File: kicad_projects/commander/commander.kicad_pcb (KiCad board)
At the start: 2 copper layers, 50 x 70 mm, 17 parts, among them J1 left input IDC14, J2 right input IDC14, J4 TPS pinout, J5 DS1020-12-6VBT1A-R, J6 PSP 3000 connector SFV4R-4STB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, J7 PSP 2000 raw pins out, J8 debug out, SW1 RESET_SWITCH, U1 Pico, U2 AQY212S

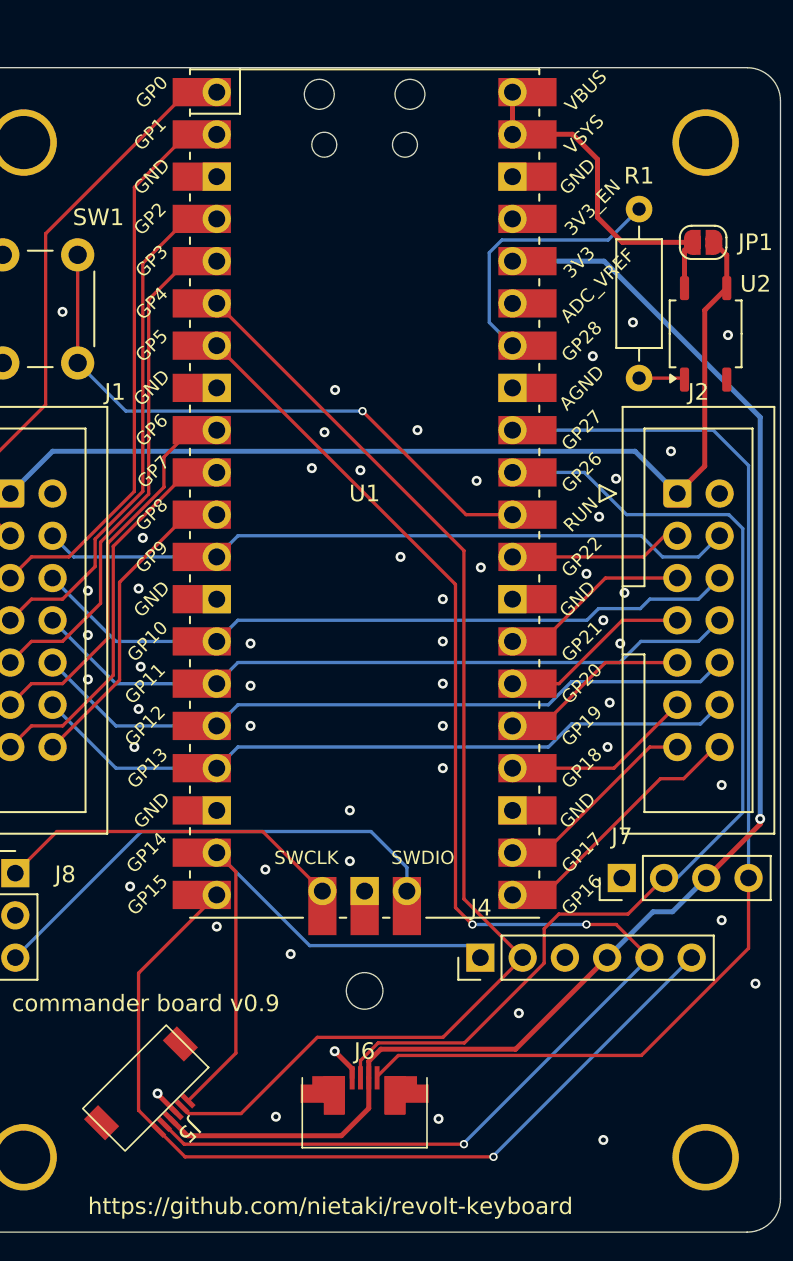
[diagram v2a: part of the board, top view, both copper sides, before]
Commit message: Clean up some vias, 0.25mm spacing of power nets for cleaner zone fills
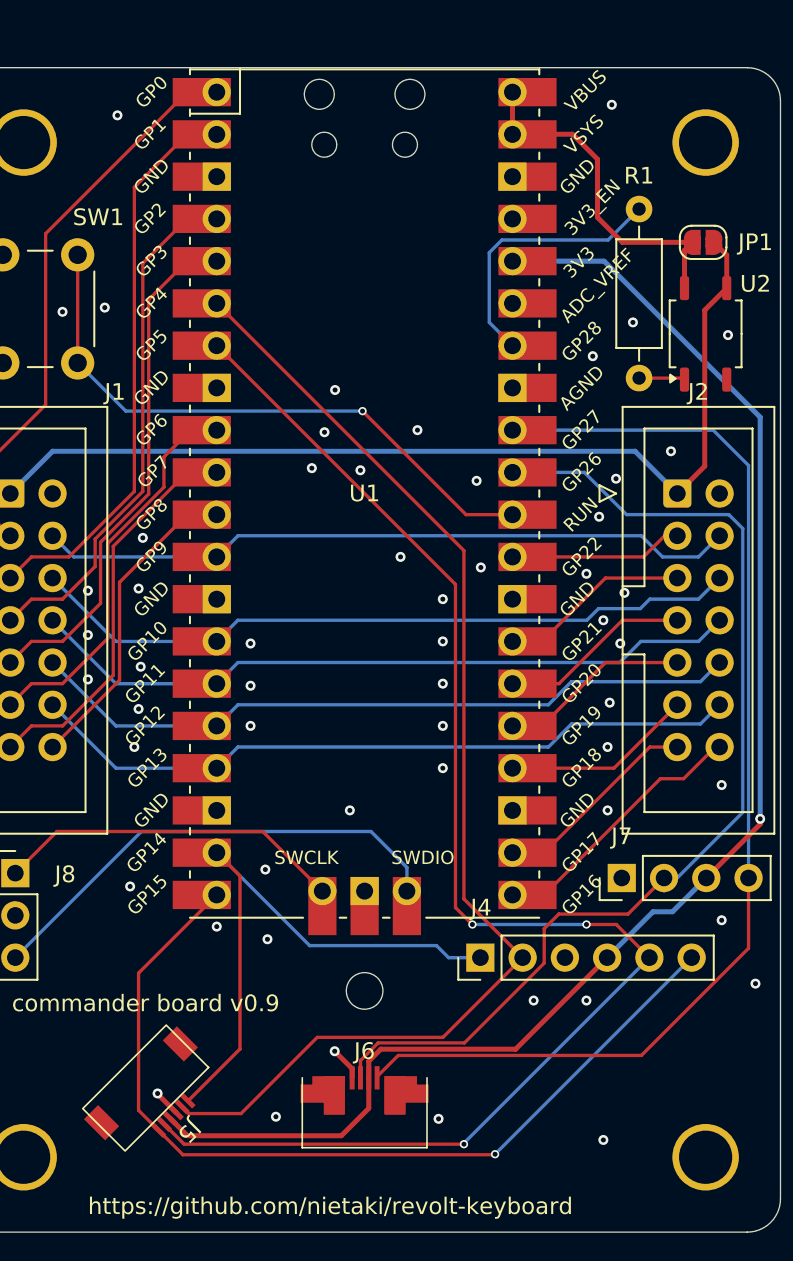
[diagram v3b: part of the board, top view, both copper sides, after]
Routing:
- net GND: vias 52 -> 56
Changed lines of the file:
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@@
   (segment (start 149 65.5) (end 149 69) (width 0.3) (layer "F.Cu") (net 26))
   (segment (start 154.23 70.97) (end 154.23 73.25) (width 0.3) (layer "F.Cu") (net 26))
-  (segment (start 127.26 108.34) (end 127.26 119.24) (width 0.2) (layer "F.Cu") (net 27))
-  (segment (start 127.26 119.24) (end 124.383883 122.116117) (width 0.2) (layer "F.Cu") (net 27))
-  (segment (start 126.11 107.19) (end 127.26 108.34) (width 0.2) (layer "F.Cu") (net 27))
+  (segment (start 127.508 108.588) (end 127.508 118.992) (width 0.2) (layer "F.Cu") (net 27))
+  (segment (start 126.11 107.19) (end 127.508 108.588) (width 0.2) (layer "F.Cu") (net 27))
+  (segment (start 127.508 118.992) (end 124.383883 122.116117) (width 0.2) (layer "F.Cu") (net 27))
   (segment (start 126.11 107.19) (end 131.696 112.776) (width 0.2) (layer "B.Cu") (net 27))
-  (segment (start 131.696 112.776) (end 141.236 112.776) (width 0.2) (layer "B.Cu") (net 27))
-  (segment (start 141.236 112.776) (end 141.96 113.5) (width 0.2) (layer "B.Cu") (net 27))
+  (segment (start 131.696 112.776) (end 139.319 112.776) (width 0.2) (layer "B.Cu") (net 27))
+  (segment (start 140.043 113.5) (end 141.96 113.5) (width 0.2) (layer "B.Cu") (net 27))
+  (segment (start 139.319 112.776) (end 140.043 113.5) (width 0.2) (layer "B.Cu") (net 27))
   (segment (start 127.568264 122.875736) (end 124.436396 122.875736) (width 0.2) (layer "F.Cu") (net 28))
   (segment (start 124.436396 122.875736) (end 124.03033 122.46967) (width 0.2) (layer "F.Cu") (net 28))
@@
   (via (at 116.84 74.676) (size 0.6) (drill 0.3) (layers "F.Cu" "B.Cu") (net 29))
   (via (at 156.464 103.124) (size 0.6) (drill 0.3) (layers "F.Cu" "B.Cu") (net 29))
-  (via (at 144.272 116.84) (size 0.6) (drill 0.3) (layers "F.Cu" "B.Cu") (net 29))
+  (via (at 149.606 104.648) (size 0.6) (drill 0.3) (layers "F.Cu" "B.Cu") (net 29))
   (via (at 122.555 121.666) (size 0.6) (drill 0.3) (layers "F.Cu" "B.Cu") (net 29))
   (via (at 139.7 99.568) (size 0.6) (drill 0.3) (layers "F.Cu" "B.Cu") (net 29))
+  (via (at 145.161 116.078) (size 0.6) (drill 0.3) (layers "F.Cu" "B.Cu") (net 29))
   (via (at 138.176 81.788) (size 0.6) (drill 0.3) (layers "F.Cu" "B.Cu") (net 29))
   (via (at 150.114 84.709) (size 0.6) (drill 0.3) (layers "F.Cu" "B.Cu") (net 29))
@@
   (via (at 139.7 97.028) (size 0.6) (drill 0.3) (layers "F.Cu" "B.Cu") (net 29))
   (via (at 126.111 111.633) (size 0.6) (drill 0.3) (layers "F.Cu" "B.Cu") (net 29))
-  (via (at 134.112 107.696) (size 0.6) (drill 0.3) (layers "F.Cu" "B.Cu") (net 29))
   (via (at 131.826 84.074) (size 0.6) (drill 0.3) (layers "F.Cu" "B.Cu") (net 29))
   (via (at 129.667 123.063) (size 0.6) (drill 0.3) (layers "F.Cu" "B.Cu") (net 29))
@@
   (via (at 148.717 77.343) (size 0.6) (drill 0.3) (layers "F.Cu" "B.Cu") (net 29))
   (via (at 121.539 96.012) (size 0.6) (drill 0.3) (layers "F.Cu" "B.Cu") (net 29))
-  (via (at 130.556 113.284) (size 0.6) (drill 0.3) (layers "F.Cu" "B.Cu") (net 29))
+  (via (at 129.159 112.395) (size 0.6) (drill 0.3) (layers "F.Cu" "B.Cu") (net 29))
   (via (at 149.098 86.995) (size 0.6) (drill 0.3) (layers "F.Cu" "B.Cu") (net 29))
   (via (at 128.143 94.615) (size 0.6) (drill 0.3) (layers "F.Cu" "B.Cu") (net 29))
@@
   (via (at 149.733 98.171) (size 0.6) (drill 0.3) (layers "F.Cu" "B.Cu") (net 29))
   (via (at 139.446 123.19) (size 0.6) (drill 0.3) (layers "F.Cu" "B.Cu") (net 29))
+  (via (at 148.336 116.078) (size 0.6) (drill 0.3) (layers "F.Cu" "B.Cu") (net 29))
   (via (at 129.032 108.204) (size 0.6) (drill 0.3) (layers "F.Cu" "B.Cu") (net 29))
   (via (at 118.364 91.44) (size 0.6) (drill 0.3) (layers "F.Cu" "B.Cu") (net 29))
@@
   (via (at 132.588 81.915) (size 0.6) (drill 0.3) (layers "F.Cu" "B.Cu") (net 29))
   (via (at 151.13 75.311) (size 0.6) (drill 0.3) (layers "F.Cu" "B.Cu") (net 29))
+  (via (at 119.38 74.422) (size 0.6) (drill 0.3) (layers "F.Cu" "B.Cu") (net 29))
   (via (at 128.143 99.568) (size 0.6) (drill 0.3) (layers "F.Cu" "B.Cu") (net 29))
+  (via (at 149.86 62.23) (size 0.6) (drill 0.3) (layers "F.Cu" "B.Cu") (net 29))
   (via (at 121.666 88.265) (size 0.6) (drill 0.3) (layers "F.Cu" "B.Cu") (net 29))
   (via (at 149.352 93.218) (size 0.6) (drill 0.3) (layers "F.Cu" "B.Cu") (net 29))
   (via (at 133.201 119.126) (size 0.6) (drill 0.3) (layers "F.Cu" "B.Cu") (net 29))
   (via (at 121.158 100.838) (size 0.6) (drill 0.3) (layers "F.Cu" "B.Cu") (net 29))
+  (via (at 120.142 62.865) (size 0.6) (drill 0.3) (layers "F.Cu" "B.Cu") (net 29))
   (via (at 150.622 91.567) (size 0.6) (drill 0.3) (layers "F.Cu" "B.Cu") (net 29))
   (via (at 133.223 79.375) (size 0.6) (drill 0.3) (layers "F.Cu" "B.Cu") (net 29))
@@
   (segment (start 152.12 113.5) (end 140.97 124.65) (width 0.2) (layer "B.Cu") (net 31))
   (segment (start 148.336 111.506) (end 141.478 111.506) (width 0.2) (layer "B.Cu") (net 31))
-  (segment (start 142.748 125.476) (end 124.208234 125.476) (width 0.2) (layer "F.Cu") (net 32))
-  (segment (start 124.208234 125.476) (end 122.616117 123.883883) (width 0.2) (layer "F.Cu") (net 32))
+  (segment (start 142.811 125.349) (end 124.081234 125.349) (width 0.2) (layer "F.Cu") (net 32))
   (segment (start 121.412 122.679766) (end 122.616117 123.883883) (width 0.2) (layer "F.Cu") (net 32))
   (segment (start 126.11 109.73) (end 121.412 114.428) (width 0.2) (layer "F.Cu") (net 32))
   (segment (start 121.412 114.428) (end 121.412 122.679766) (width 0.2) (layer "F.Cu") (net 32))
-  (via (at 142.748 125.476) (size 0.5) (drill 0.3) (layers "F.Cu" "B.Cu") (net 32))
-  (segment (start 142.748 125.412) (end 142.748 125.476) (width 0.2) (layer "B.Cu") (net 32))
-  (segment (start 154.66 113.5) (end 142.748 125.412) (width 0.2) (layer "B.Cu") (net 32))
+  (segment (start 142.843 125.317) (end 142.811 125.349) (width 0.2) (layer "F.Cu") (net 32))
+  (segment (start 124.081234 125.349) (end 122.616117 123.883883) (width 0.2) (layer "F.Cu") (net 32))
+  (via (at 142.843 125.317) (size 0.5) (drill 0.3) (layers "F.Cu" "B.Cu") (net 32))
+  (segment (start 142.843 125.317) (end 154.66 113.5) (width 0.2) (layer "B.Cu") (net 32))
   (segment (start 151.638 119.38) (end 158.08 112.938) (width 0.2) (layer "F.Cu") (net 33))
   (segment (start 135.75 120.725) (end 135.75 120.650736) (width 0.2) (layer "F.Cu") (net 33))

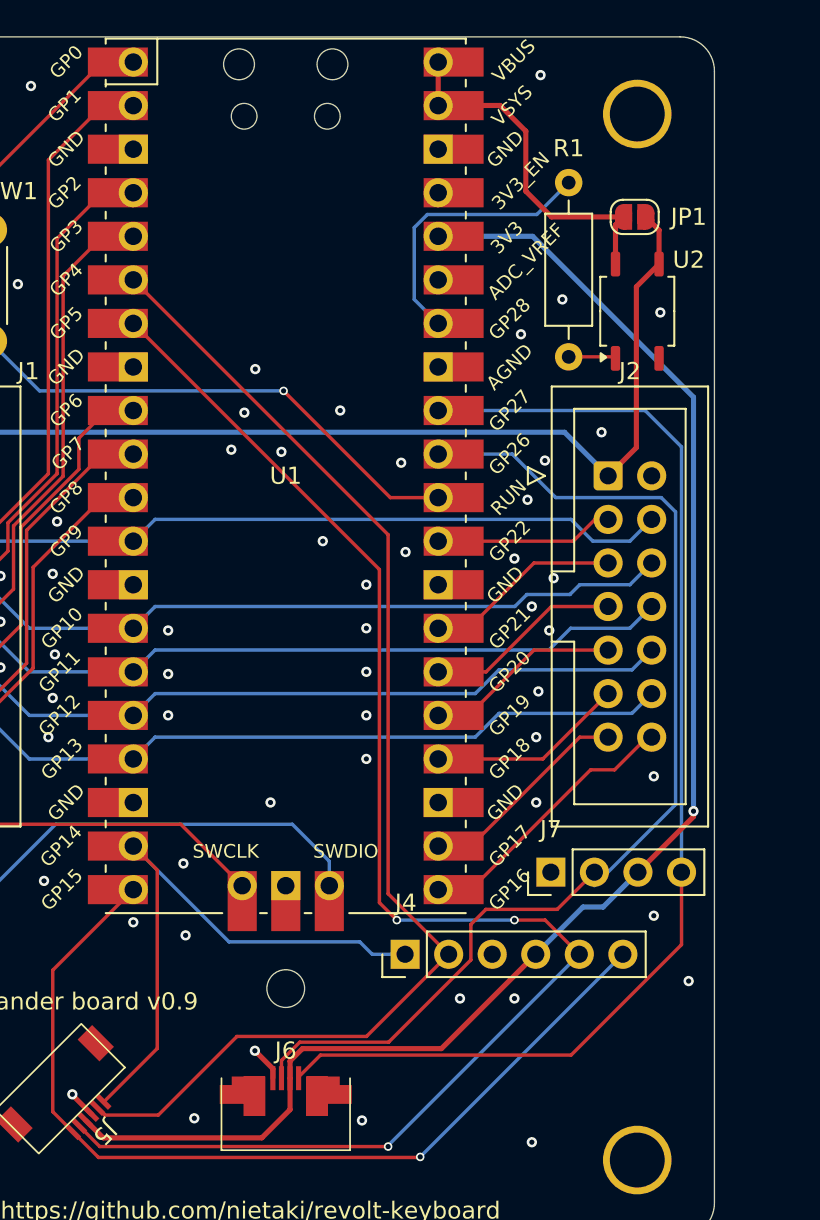
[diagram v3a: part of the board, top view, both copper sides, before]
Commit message: Replace a relay with a MOSFET (like a pro)
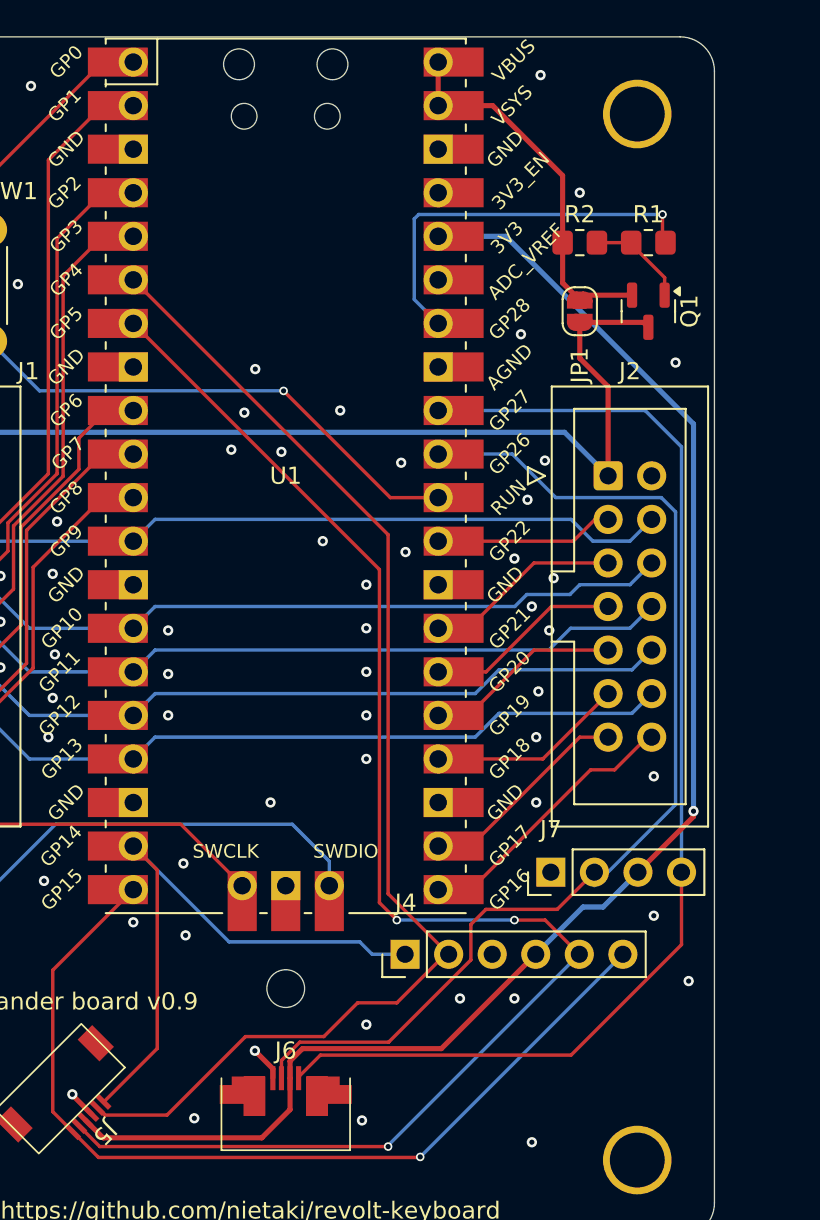
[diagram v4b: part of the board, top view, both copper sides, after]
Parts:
- removed U2: AQY212S, Package_SO:SOP-4_3.8x4.1mm_P2.54mm
- added Q1: MMFTP3401, Package_TO_SOT_SMD:SOT-23, F.Cu at (156.1, 76.0)
- added R2: 10k, Resistor_SMD:R_0805_2012Metric_Pad1.20x1.40mm_HandSolder, F.Cu at (152.1, 72.0)
- R1: value 200R -> 220R; footprint Resistor_THT:R_Axial_DIN0207_L6.3mm_D2.5mm_P10.16mm_Horizontal -> Resistor_SMD:R_0805_2012Metric_Pad1.20x1.40mm_HandSolder
- moved R1 8.12 mm to (156.1, 72.0), turned to 0 degrees
- moved JP1 6.37 mm to (152.1, 76.0), turned to -90 degrees
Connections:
- net /LED_ENABLE renamed /NOT_LED_ENABLE
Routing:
- net /NOT_LED_ENABLE: track 16.3 -> 23.0 mm, vias 0 -> 1
- net 5V: track 21.0 -> 24.2 mm
- net Net-(Q1-G): track 2.77 -> 5.87 mm
- net LED_5V: track 58.9 -> 56.0 mm
- net 3V3: track 88.5 -> 87.6 mm
